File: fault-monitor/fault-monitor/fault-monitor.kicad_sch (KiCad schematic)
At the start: 15 parts, among them J1 Conn_01x03, J2 Conn_01x06, J3 Conn_01x02, J4 Conn_01x02, U1 ESP32-DevKitC

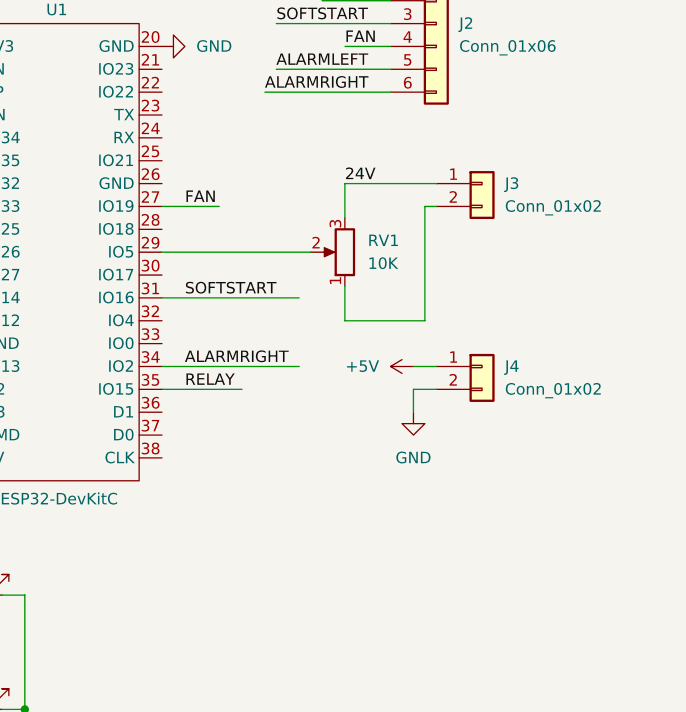
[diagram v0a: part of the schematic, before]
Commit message: add jumper and test pad
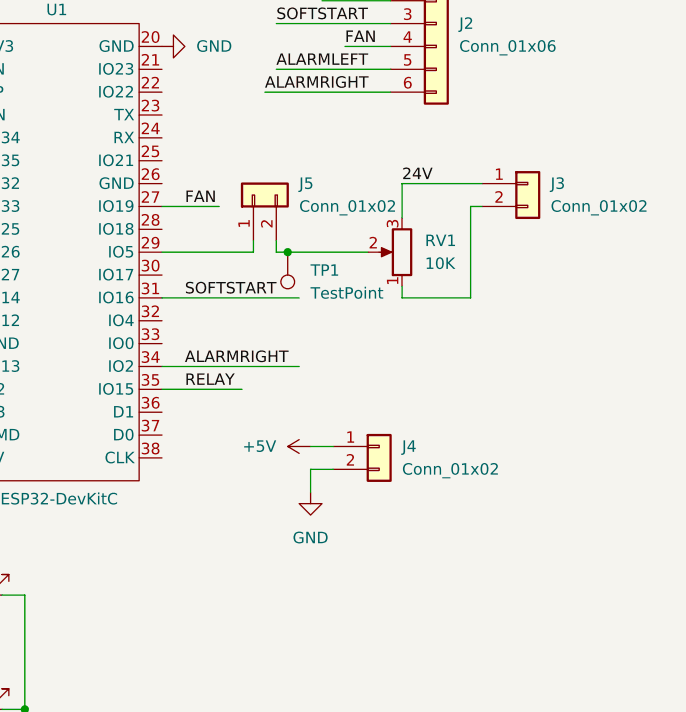
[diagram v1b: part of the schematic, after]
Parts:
- added J5: Conn_01x02, symbol Connector_Generic:Conn_01x02
- added TP1: TestPoint, symbol Connector:TestPoint
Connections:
- net at RV1.2: now also J5.2 (Pin_2), TP1.1; no longer U1.29 (IO5)
- new net: J5.1 (Pin_1), U1.29 (IO5)
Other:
- moved on the sheet: J3, J4, RV1

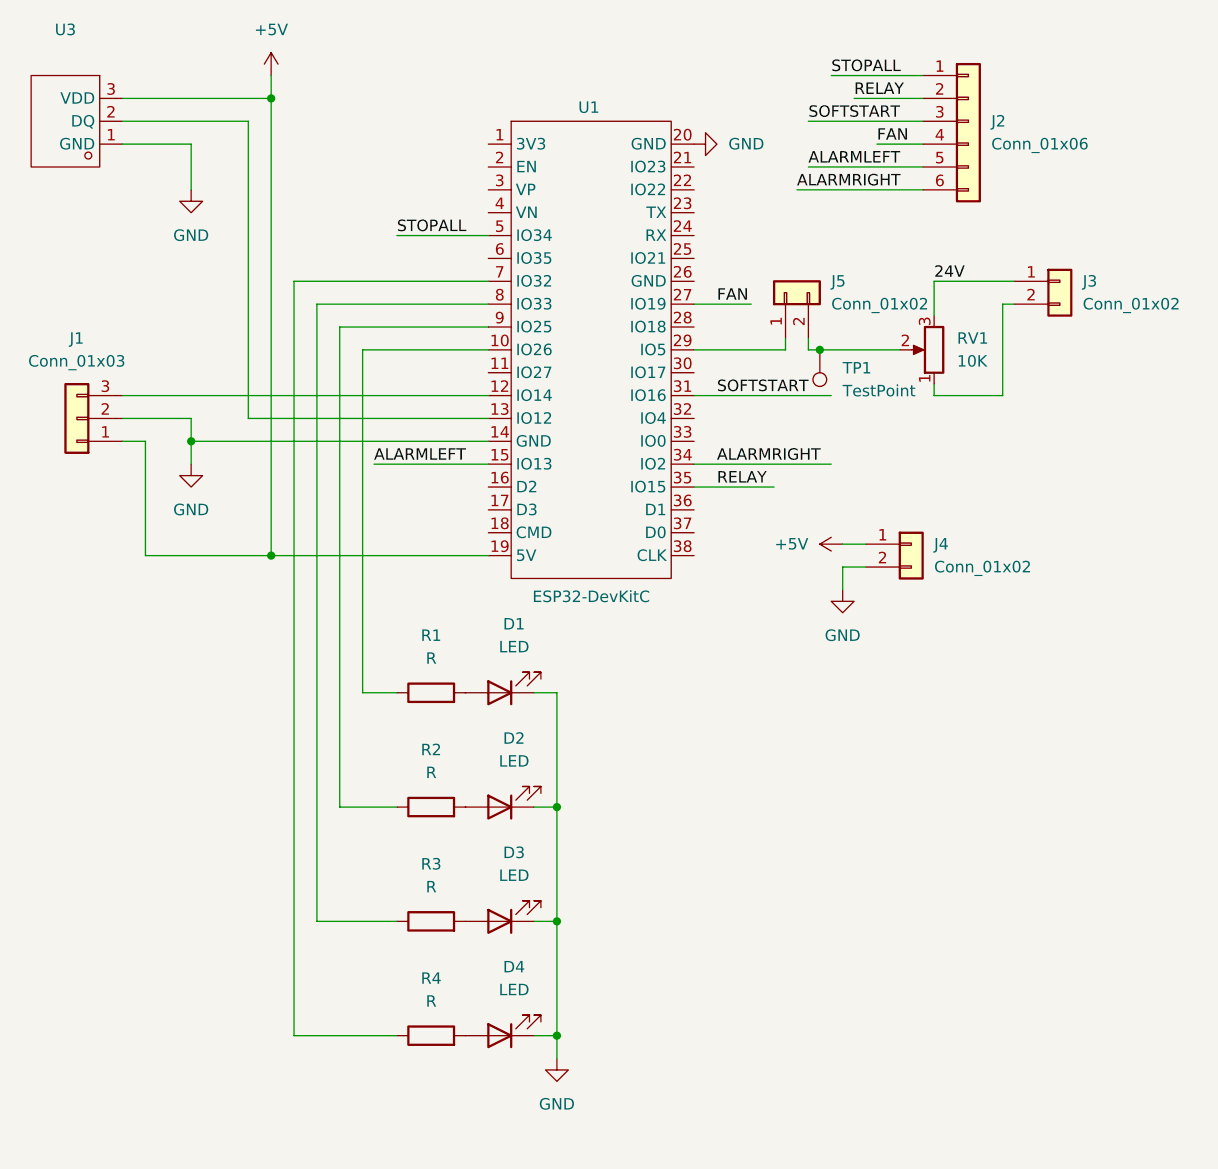
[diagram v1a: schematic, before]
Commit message: add extra IO pins
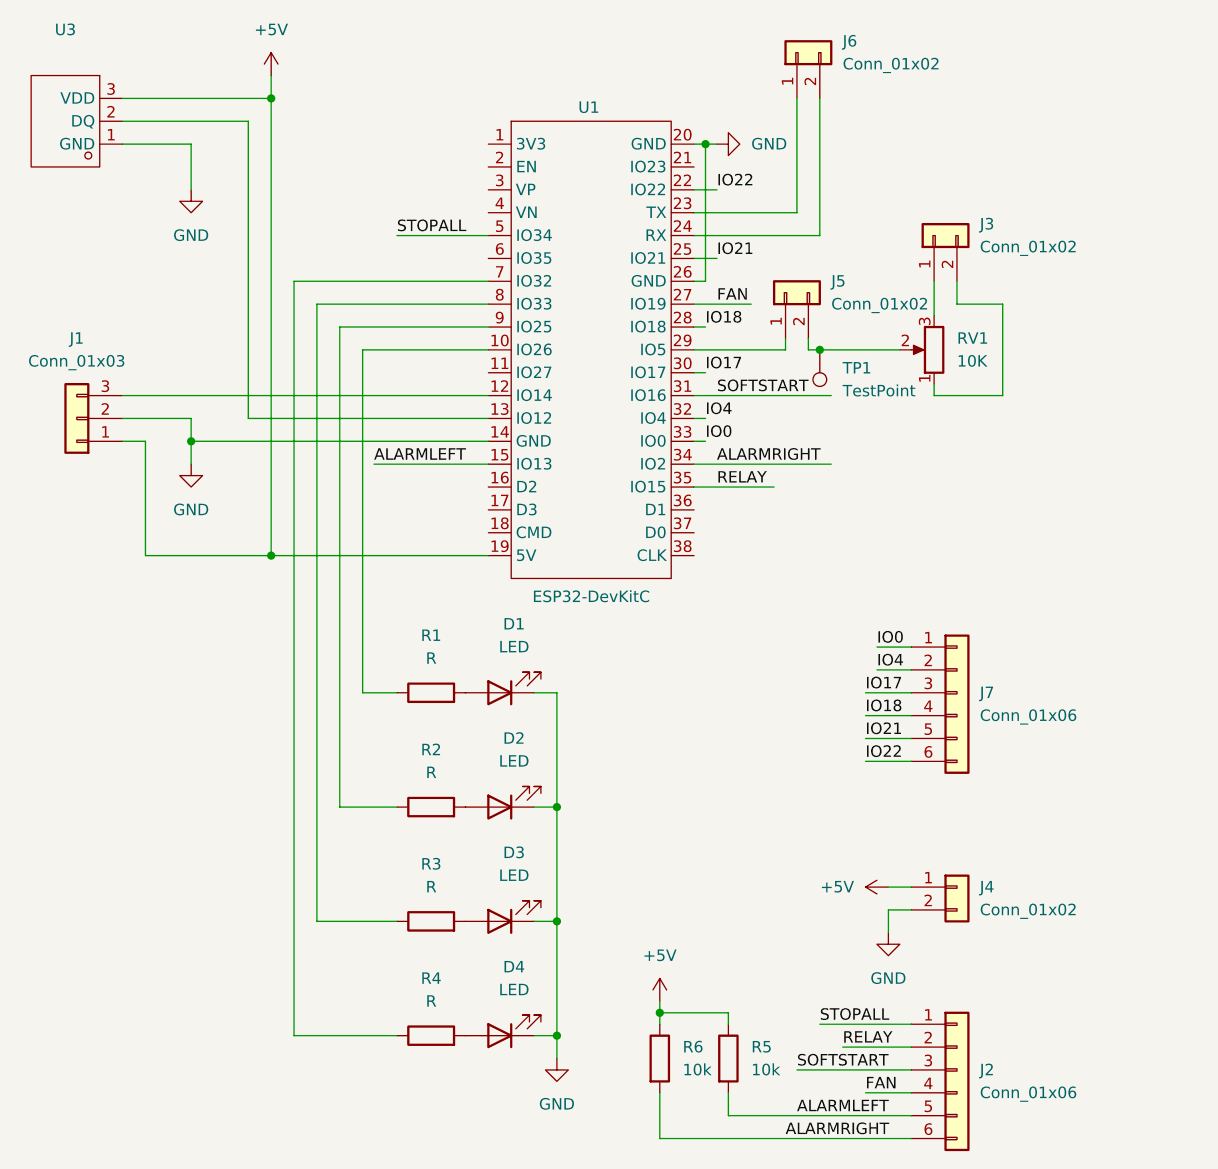
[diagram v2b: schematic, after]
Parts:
- added J6: Conn_01x02, symbol Connector_Generic:Conn_01x02
- added J7: Conn_01x06, symbol Connector_Generic:Conn_01x06
- added R5, R6: 10k, symbol Device:R
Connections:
- net +5V: now also R5.1, R6.1
- net ALARMLEFT: now also R5.2
- net ALARMRIGHT: now also R6.2
- net GND: now also U1.26 (GND)
- net IO22: now reaches U1.22 (IO22)
- net IO22: now also J7.6 (Pin_6)
- net at U1.23 (TX): now also J6.1 (Pin_1)
- net at U1.24 (RX): now also J6.2 (Pin_2)
- net IO21: now reaches U1.25 (IO21)
- net IO21: now also J7.5 (Pin_5)
- net IO18: now reaches U1.28 (IO18)
- net IO18: now also J7.4 (Pin_4)
- net IO17: now reaches U1.30 (IO17)
- net IO17: now also J7.3 (Pin_3)
- net IO4: now reaches U1.32 (IO4)
- net IO4: now also J7.2 (Pin_2)
- net IO0: now reaches U1.33 (IO0)
- net IO0: now also J7.1 (Pin_1)
- net 24V: no longer names the net of J3.1 (Pin_1), RV1.3
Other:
- moved on the sheet: J2, J3, J4

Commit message: assign footprints
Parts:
- D1, D2, D3, D4: footprint (none) -> LED_THT:LED_D5.0mm
- J1: footprint (none) -> Connector_Wago:Wago_734-133_1x03_P3.50mm_Vertical
- J2, J7: footprint (none) -> Connector_Wago:Wago_734-136_1x06_P3.50mm_Vertical
- J3, J4, J6: footprint (none) -> Connector_Wago:Wago_734-132_1x02_P3.50mm_Vertical
- J5: footprint (none) -> Connector_PinHeader_2.54mm:PinHeader_1x02_P2.54mm_Vertical
- R1, R2, R3, R4: value R -> 2.2k; footprint (none) -> Resistor_THT:R_Axial_DIN0207_L6.3mm_D2.5mm_P10.16mm_Horizontal
- R5, R6, RV1: footprint (none) -> Resistor_THT:R_Axial_DIN0207_L6.3mm_D2.5mm_P10.16mm_Horizontal
- TP1: footprint (none) -> Connector_PinHeader_2.54mm:PinHeader_1x01_P2.54mm_Vertical
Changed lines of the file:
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@@
 			)
 		)
-		(property "Footprint" ""
+		(property "Footprint" "Connector_PinHeader_2.54mm:PinHeader_1x01_P2.54mm_Vertical"
 			(at 104.14 50.8 0)
 			(effects
@@
 			)
 		)
-		(property "Footprint" ""
+		(property "Footprint" "Connector_PinHeader_2.54mm:PinHeader_1x02_P2.54mm_Vertical"
 			(at 105.41 44.45 0)
 			(effects
@@
 			)
 		)
-		(property "Footprint" ""
+		(property "Footprint" "Connector_Wago:Wago_734-136_1x06_P3.50mm_Vertical"
 			(at 124.46 130.81 0)
 			(effects
@@
 			)
 		)
-		(property "Footprint" ""
+		(property "Footprint" "Connector_Wago:Wago_734-132_1x02_P3.50mm_Vertical"
 			(at 124.46 110.49 0)
 			(effects
@@
 			)
 		)
-		(property "Value" "R"
+		(property "Value" "2.2k"
 			(at 66.04 97.79 90)
 			(effects
@@
 			)
 		)
-		(property "Footprint" ""
+		(property "Footprint" "Resistor_THT:R_Axial_DIN0207_L6.3mm_D2.5mm_P10.16mm_Horizontal"
 			(at 66.04 103.378 90)
 			(effects
@@
 			)
 		)
-		(property "Footprint" ""
+		(property "Footprint" "Resistor_THT:R_Axial_DIN0207_L6.3mm_D2.5mm_P10.16mm_Horizontal"
 			(at 89.662 129.54 90)
 			(effects
@@
 			)
 		)
-		(property "Value" "R"
+		(property "Value" "2.2k"
 			(at 66.04 123.19 90)
 			(effects
@@
 			)
 		)
-		(property "Footprint" ""
+		(property "Footprint" "Resistor_THT:R_Axial_DIN0207_L6.3mm_D2.5mm_P10.16mm_Horizontal"
 			(at 66.04 128.778 90)
 			(effects
@@
 			)
 		)
-		(property "Footprint" ""
+		(property "Footprint" "LED_THT:LED_D5.0mm"
 			(at 73.66 114.3 0)
 			(effects
@@
 			)
 		)
-		(property "Footprint" ""
+		(property "Footprint" "Connector_Wago:Wago_734-132_1x02_P3.50mm_Vertical"
 			(at 106.68 17.78 0)
 			(effects
@@
 			)
 		)
-		(property "Footprint" ""
+		(property "Footprint" "Connector_Wago:Wago_734-132_1x02_P3.50mm_Vertical"
 			(at 121.92 38.1 0)
 			(effects
@@
 			)
 		)
-		(property "Footprint" ""
+		(property "Footprint" "LED_THT:LED_D5.0mm"
 			(at 73.66 127 0)
 			(effects
@@
 			)
 		)
-		(property "Footprint" ""
+		(property "Footprint" "Connector_Wago:Wago_734-133_1x03_P3.50mm_Vertical"
 			(at 26.67 58.42 0)
 			(effects
@@
 			)
 		)
-		(property "Value" "R"
+		(property "Value" "2.2k"
 			(at 66.04 85.09 90)
 			(effects
@@
 			)
 		)
-		(property "Footprint" ""
+		(property "Footprint" "Resistor_THT:R_Axial_DIN0207_L6.3mm_D2.5mm_P10.16mm_Horizontal"
 			(at 66.04 90.678 90)
 			(effects
@@
 			)
 		)
-		(property "Footprint" ""
+		(property "Footprint" "LED_THT:LED_D5.0mm"
 			(at 73.66 101.6 0)
 			(effects
@@
 			)
 		)
-		(property "Footprint" ""
+		(property "Footprint" "LED_THT:LED_D5.0mm"
 			(at 73.66 88.9 0)
 			(effects
@@
 			)
 		)
-		(property "Footprint" ""
+		(property "Footprint" "Connector_Wago:Wago_734-136_1x06_P3.50mm_Vertical"
 			(at 124.46 88.9 0)
 			(effects
@@
 			)
 		)
-		(property "Footprint" ""
+		(property "Footprint" "Resistor_THT:R_Axial_DIN0207_L6.3mm_D2.5mm_P10.16mm_Horizontal"
 			(at 97.282 129.54 90)
 			(effects
@@
 			)
 		)
-		(property "Value" "R"
+		(property "Value" "2.2k"
 			(at 66.04 110.49 90)
 			(effects
@@
 			)
 		)
-		(property "Footprint" ""
+		(property "Footprint" "Resistor_THT:R_Axial_DIN0207_L6.3mm_D2.5mm_P10.16mm_Horizontal"
 			(at 66.04 116.078 90)
 			(effects
@@
 			)
 		)
-		(property "Footprint" ""
+		(property "Footprint" "Resistor_THT:R_Axial_DIN0207_L6.3mm_D2.5mm_P10.16mm_Horizontal"
 			(at 121.92 50.8 0)
 			(effects

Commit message: Initial board layout
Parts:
- RV1: footprint Resistor_THT:R_Axial_DIN0207_L6.3mm_D2.5mm_P10.16mm_Horizontal -> Potentiometer_THT:Potentiometer_ACP_CA9-V10_Vertical
- U1: footprint ProPrj_Fau-easyedapro:BULETM-SMD_ESP32-DEVKITC -> PCM_Espressif:ESP32-DevKitC
- U3: footprint ProPrj_Fau-easyedapro:TO-92-3_L4.5-W3.5-P1.27-L -> Package_TO_SOT_THT:TO-92L
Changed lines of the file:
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@@
 			)
 		)
-		(property "Footprint" "ProPrj_Fau-easyedapro:TO-92-3_L4.5-W3.5-P1.27-L"
+		(property "Footprint" "Package_TO_SOT_THT:TO-92L"
 			(at 26.67 25.4 0)
 			(effects
@@
 			)
 		)
-		(property "Footprint" "Resistor_THT:R_Axial_DIN0207_L6.3mm_D2.5mm_P10.16mm_Horizontal"
+		(property "Footprint" "Potentiometer_THT:Potentiometer_ACP_CA9-V10_Vertical"
 			(at 121.92 50.8 0)
 			(effects
@@
 			)
 		)
-		(property "Footprint" "ProPrj_Fau-easyedapro:BULETM-SMD_ESP32-DEVKITC"
+		(property "Footprint" "PCM_Espressif:ESP32-DevKitC"
 			(at 83.82 50.8 0)
 			(effects

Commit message: use wago lever terminal blocks
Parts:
- J1: footprint Connector_Wago:Wago_734-133_1x03_P3.50mm_Vertical -> TerminalBlock_WAGO:TerminalBlock_WAGO_2601-1103_1x03_P3.50mm_Horizontal
- J2, J7: footprint Connector_Wago:Wago_734-136_1x06_P3.50mm_Vertical -> TerminalBlock_WAGO:TerminalBlock_WAGO_2601-1106_1x06_P3.50mm_Horizontal
- J3, J4, J6: footprint Connector_Wago:Wago_734-132_1x02_P3.50mm_Vertical -> TerminalBlock_WAGO:TerminalBlock_WAGO_2601-1102_1x02_P3.50mm_Horizontal
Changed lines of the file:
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@@
 			)
 		)
-		(property "Footprint" "Connector_Wago:Wago_734-136_1x06_P3.50mm_Vertical"
+		(property "Footprint" "TerminalBlock_WAGO:TerminalBlock_WAGO_2601-1106_1x06_P3.50mm_Horizontal"
 			(at 124.46 130.81 0)
 			(effects
@@
 			)
 		)
-		(property "Footprint" "Connector_Wago:Wago_734-132_1x02_P3.50mm_Vertical"
+		(property "Footprint" "TerminalBlock_WAGO:TerminalBlock_WAGO_2601-1102_1x02_P3.50mm_Horizontal"
 			(at 124.46 110.49 0)
 			(effects
@@
 			)
 		)
-		(property "Footprint" "Connector_Wago:Wago_734-132_1x02_P3.50mm_Vertical"
+		(property "Footprint" "TerminalBlock_WAGO:TerminalBlock_WAGO_2601-1102_1x02_P3.50mm_Horizontal"
 			(at 106.68 17.78 0)
 			(effects
@@
 			)
 		)
-		(property "Footprint" "Connector_Wago:Wago_734-132_1x02_P3.50mm_Vertical"
+		(property "Footprint" "TerminalBlock_WAGO:TerminalBlock_WAGO_2601-1102_1x02_P3.50mm_Horizontal"
 			(at 121.92 38.1 0)
 			(effects
@@
 			)
 		)
-		(property "Footprint" "Connector_Wago:Wago_734-133_1x03_P3.50mm_Vertical"
+		(property "Footprint" "TerminalBlock_WAGO:TerminalBlock_WAGO_2601-1103_1x03_P3.50mm_Horizontal"
 			(at 26.67 58.42 0)
 			(effects
@@
 			)
 		)
-		(property "Footprint" "Connector_Wago:Wago_734-136_1x06_P3.50mm_Vertical"
+		(property "Footprint" "TerminalBlock_WAGO:TerminalBlock_WAGO_2601-1106_1x06_P3.50mm_Horizontal"
 			(at 124.46 88.9 0)
 			(effects

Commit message: route pcb
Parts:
- U1: footprint PCM_Espressif:ESP32-DevKitC -> PCM_Espressif:ESP32-DevKitC-ReversePinOrder
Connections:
- net IO0: now also J7.6 (Pin_6); no longer J7.1 (Pin_1)
- net IO17: now also J7.4 (Pin_4); no longer J7.3 (Pin_3)
- net IO18: now also J7.3 (Pin_3); no longer J7.4 (Pin_4)
- net IO21: now also J7.2 (Pin_2); no longer J7.5 (Pin_5)
- net IO22: now also J7.1 (Pin_1); no longer J7.6 (Pin_6)
- net IO4: now also J7.5 (Pin_5); no longer J7.2 (Pin_2)
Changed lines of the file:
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@@
 	(symbol
 		(lib_id "Connector_Generic:Conn_01x06")
-		(at 124.46 88.9 0)
-		(unit 1)
-		(exclude_from_sim no)
-		(in_bom yes)
-		(on_board yes)
-		(dnp no)
-		(fields_autoplaced yes)
+		(at 124.46 91.44 0)
+		(mirror x)
+		(unit 1)
+		(exclude_from_sim no)
+		(in_bom yes)
+		(on_board yes)
+		(dnp no)
 		(property "Reference" "J7"
-			(at 127 88.8999 0)
+			(at 127 91.4401 0)
 			(effects
 				(font
@@
 		)
 		(property "Value" "Conn_01x06"
-			(at 127 91.4399 0)
+			(at 127 88.9001 0)
 			(effects
 				(font
@@
 		)
 		(property "Footprint" "TerminalBlock_WAGO:TerminalBlock_WAGO_2601-1106_1x06_P3.50mm_Horizontal"
-			(at 124.46 88.9 0)
+			(at 124.46 91.44 0)
 			(effects
 				(font
@@
 		)
 		(property "Datasheet" "~"
-			(at 124.46 88.9 0)
+			(at 124.46 91.44 0)
 			(effects
 				(font
@@
 		)
 		(property "Description" "Generic connector, single row, 01x06, script generated (kicad-library-utils/schlib/autogen/connector/)"
-			(at 124.46 88.9 0)
+			(at 124.46 91.44 0)
 			(effects
 				(font
@@
 		)
 		(instances
-			(project ""
+			(project "fault-monitor"
 				(path "/64884559-cbe4-442b-837a-f1967fbf7136"
 					(reference "J7")
@@
 			)
 		)
-		(property "Footprint" "PCM_Espressif:ESP32-DevKitC"
+		(property "Footprint" "PCM_Espressif:ESP32-DevKitC-ReversePinOrder"
 			(at 83.82 50.8 0)
 			(effects

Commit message: add wago 3d models
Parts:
- J1: footprint TerminalBlock_WAGO:TerminalBlock_WAGO_2601-1103_1x03_P3.50mm_Horizontal -> TerminalBlock_WAGO_3D:TerminalBlock_WAGO_2601-1103_1x03_P3.50mm_Horizontal-3D
- J2, J7: footprint TerminalBlock_WAGO:TerminalBlock_WAGO_2601-1106_1x06_P3.50mm_Horizontal -> TerminalBlock_WAGO_3D:TerminalBlock_WAGO_2601-1106_1x06_P3.50mm_Horizontal-3D
- J3, J4, J6: footprint TerminalBlock_WAGO:TerminalBlock_WAGO_2601-1102_1x02_P3.50mm_Horizontal -> TerminalBlock_WAGO_3D:TerminalBlock_WAGO_2601-1102_1x02_P3.50mm_Horizontal-3D
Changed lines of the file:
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@@
 			)
 		)
-		(property "Footprint" "TerminalBlock_WAGO:TerminalBlock_WAGO_2601-1106_1x06_P3.50mm_Horizontal"
+		(property "Footprint" "TerminalBlock_WAGO_3D:TerminalBlock_WAGO_2601-1106_1x06_P3.50mm_Horizontal-3D"
 			(at 124.46 130.81 0)
 			(effects
@@
 			)
 		)
-		(property "Footprint" "TerminalBlock_WAGO:TerminalBlock_WAGO_2601-1102_1x02_P3.50mm_Horizontal"
+		(property "Footprint" "TerminalBlock_WAGO_3D:TerminalBlock_WAGO_2601-1102_1x02_P3.50mm_Horizontal-3D"
 			(at 124.46 110.49 0)
 			(effects
@@
 			)
 		)
-		(property "Footprint" "TerminalBlock_WAGO:TerminalBlock_WAGO_2601-1102_1x02_P3.50mm_Horizontal"
+		(property "Footprint" "TerminalBlock_WAGO_3D:TerminalBlock_WAGO_2601-1102_1x02_P3.50mm_Horizontal-3D"
 			(at 106.68 17.78 0)
 			(effects
@@
 			)
 		)
-		(property "Footprint" "TerminalBlock_WAGO:TerminalBlock_WAGO_2601-1102_1x02_P3.50mm_Horizontal"
+		(property "Footprint" "TerminalBlock_WAGO_3D:TerminalBlock_WAGO_2601-1102_1x02_P3.50mm_Horizontal-3D"
 			(at 121.92 38.1 0)
 			(effects
@@
 			)
 		)
-		(property "Footprint" "TerminalBlock_WAGO:TerminalBlock_WAGO_2601-1103_1x03_P3.50mm_Horizontal"
+		(property "Footprint" "TerminalBlock_WAGO_3D:TerminalBlock_WAGO_2601-1103_1x03_P3.50mm_Horizontal-3D"
 			(at 26.67 58.42 0)
 			(effects
@@
 			)
 		)
-		(property "Footprint" "TerminalBlock_WAGO:TerminalBlock_WAGO_2601-1106_1x06_P3.50mm_Horizontal"
+		(property "Footprint" "TerminalBlock_WAGO_3D:TerminalBlock_WAGO_2601-1106_1x06_P3.50mm_Horizontal-3D"
 			(at 124.46 91.44 0)
 			(effects

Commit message: update to use real parts we will order
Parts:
- RV1: footprint Potentiometer_THT:Potentiometer_ACP_CA9-V10_Vertical -> DigiKey:POT_N6L30T0N_AMP
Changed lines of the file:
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@@
 			)
 		)
-		(property "Footprint" "Potentiometer_THT:Potentiometer_ACP_CA9-V10_Vertical"
+		(property "Footprint" "DigiKey:POT_N6L30T0N_AMP"
 			(at 121.92 50.8 0)
 			(effects
